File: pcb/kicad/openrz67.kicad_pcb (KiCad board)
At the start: 2 copper layers, 48 x 22 mm, 63 parts, among them K1 G6K-2F-Y DC3, K2 G6K-2F-Y DC3, Q1 DTC114EKAT146, Q2 DTC114EKAT146, U1 ESP32-C3FH4, U3 LGS5500EP, U4 S4B-XH-A(LF)(SN), X1 40MHz, X2 32.768kHz

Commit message: KiCad: archive rev-1 files, add 3D models, 0.3 mm edge clearance, cleanup
- move 2025-09-23 fabrication files and EasyEDA exports to pcb/archive/
- fetch LCSC 3D models with easyeda2kicad (tools/fetch_3d.sh); .wrl committed,
  .step gitignored; footprints repointed from dangling EASYEDA_MODELS paths
- copper-to-edge 0.30 mm with a .kicad_dru exemption for the USB-C pads
- remove two dangling vias and a 0.1 mm track stub; move two USB1 polygons
  the importer put on Edge.Cuts to F.Fab
- bottom silkscreen: OpenRZ67 Trigger v2 / 2026-09
- regenerate out/ (gerber zip, pos, BOM, PDF, renders, DRC report)
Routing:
- net VCC: vias 11 -> 10
- net +5V_VIN: vias 3 -> 2
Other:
- board text added: "OpenRZ67 Trigger v2 2026-09"
- board text removed: "EPS32-C3 Camera Trigger V1.0 2025-08-23"

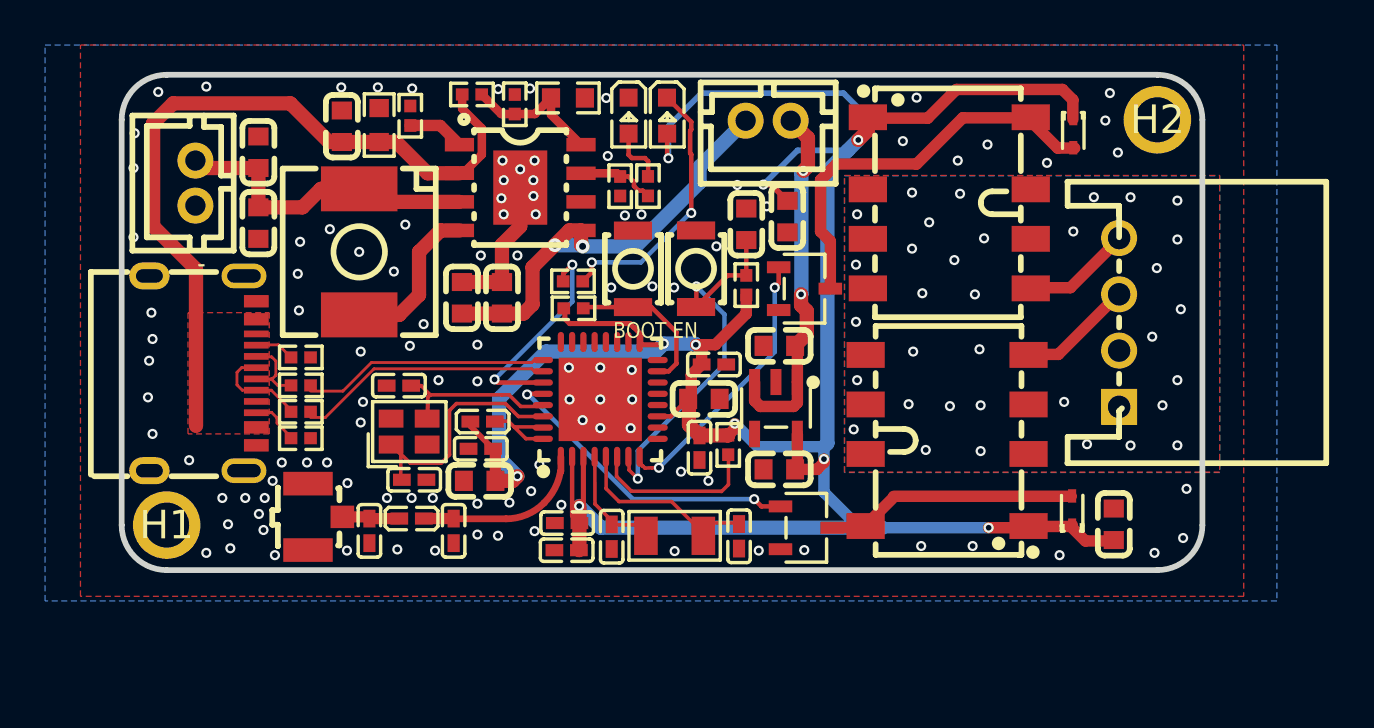
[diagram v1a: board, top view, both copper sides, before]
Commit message: KiCad: proper ERC pin types, mounting-hole symbols, courtyards, silk cleanup
- pin electrical types for ESP32-C3, LGS5500, ME6211 and USB-C; passives passive;
  PWR_FLAGs on GND/AGND/BAT+/VBUS/+5V_VIN/VDDA; ERC severities back to default
  (0 errors, 8 harmless dangling-wire warnings)
- symbol library pruned to the parts in use, embedded copies regenerated
- H1/H2: MountingHole symbols + MountingHole_2.0mm_Pad3.0 footprint, linked
- courtyards rebuilt from pads/body (+0.05 mm); 0402/0603 and overhanging
  connector silk moved to F.Fab; BOOT/EN label moved above the buttons
- tools/fetch_3d.sh bootstraps easyeda2kicad via uvx/pipx/venv; tools/export_step.sh
- DRC 0 errors / 0 unconnected / parity clean; 6 courtyard warnings remain
  where neighbours sit closer than 0.1 mm on the fabricated layout
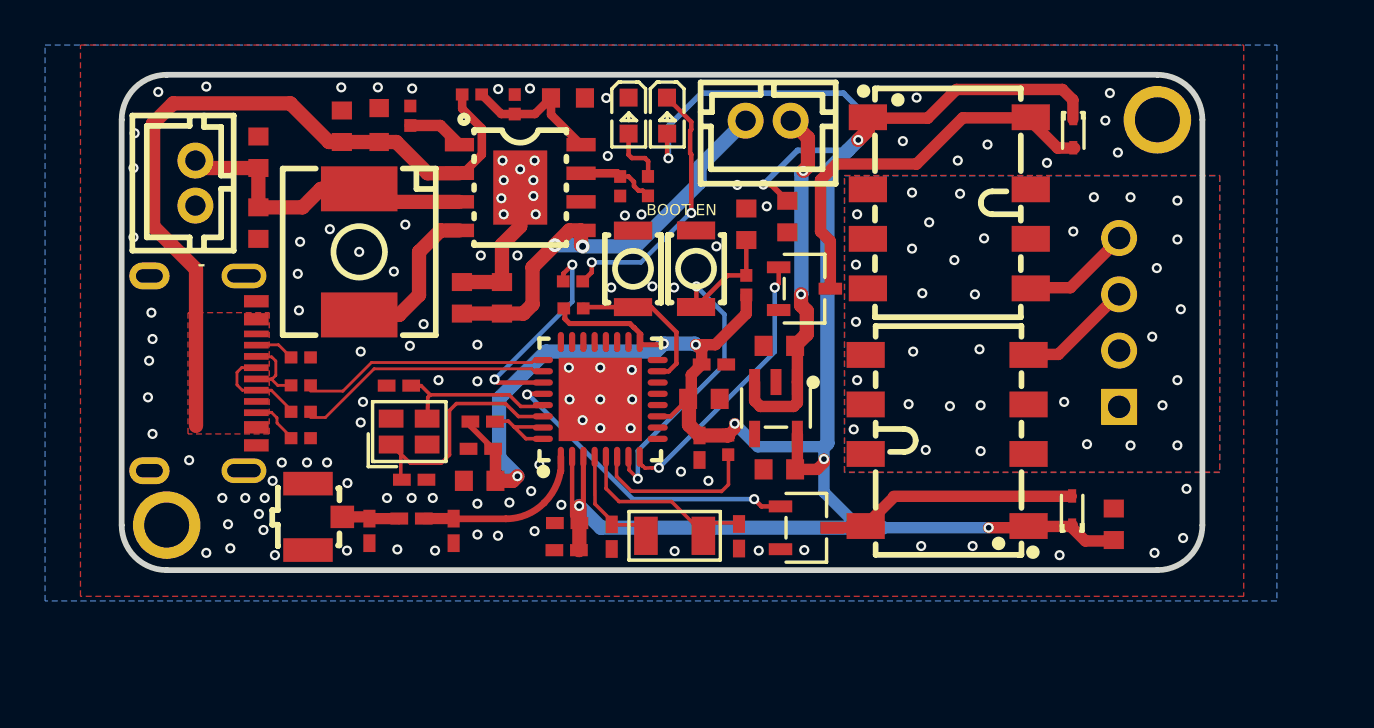
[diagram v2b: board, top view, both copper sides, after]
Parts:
- H1: value (none) -> MountingHole; footprint openrz67:Pad_e169 -> openrz67:MountingHole_2.0mm_Pad3.0
- H2: value (none) -> MountingHole; footprint openrz67:Pad_e170 -> openrz67:MountingHole_2.0mm_Pad3.0

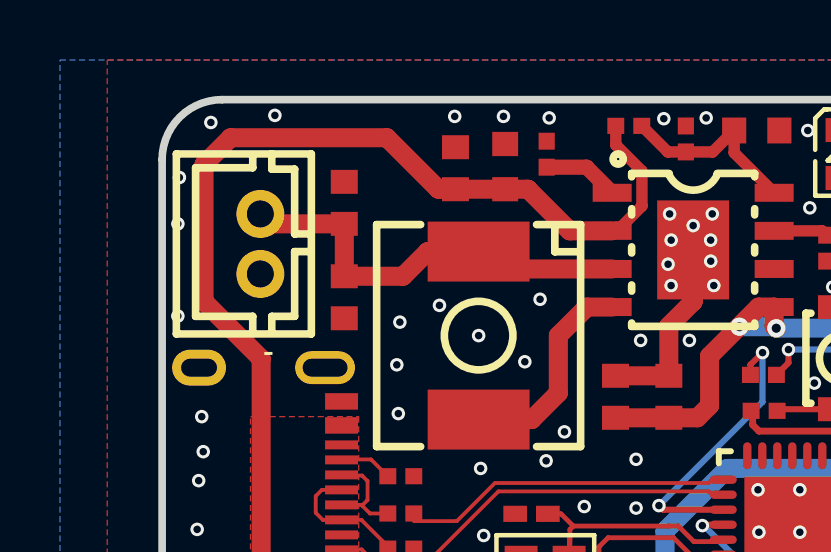
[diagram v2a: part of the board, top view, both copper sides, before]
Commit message: Rev 2: battery connector on the bottom side, facing inward
BAT1 changes from the vertical THT B2B-PH-K-S to the SMD side-entry
S2B-PH-SM4-TB (LCSC C295747) on B.Cu at the left end, opening toward the
board centre, so the cell lies flat under the PCB and plugs in without a
lead bend. BAT+ is brought down with a 0.6/0.3 via next to C22; GND uses the
bottom pour. Five GND stitching vias under the new pads removed; bottom
silkscreen labels relocated. Symbol, footprint and 3D model added to the
project libraries. DRC 0 errors, parity clean; ERC unchanged.
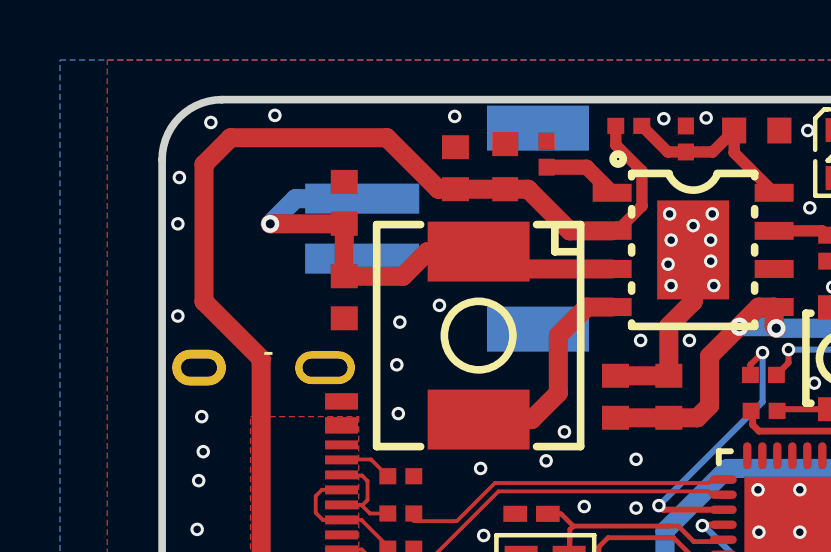
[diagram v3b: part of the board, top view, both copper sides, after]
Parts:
- BAT1: value B2B-PH-K-S(LF)(SN) -> S2B-PH-SM4-TB(LF)(SN); footprint openrz67:CONN-TH_B2B-PH-K-S -> openrz67:CONN-SMD_P2.00_S2B-PH-SM4-TB-LF-SN; moved to B.Cu
- moved BAT1 6.35 mm to (129.6, 94.3), turned to -90 degrees
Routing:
- net BAT+: track 14.2 -> 17.1 mm, vias 0 -> 1
- net GND: vias 108 -> 103

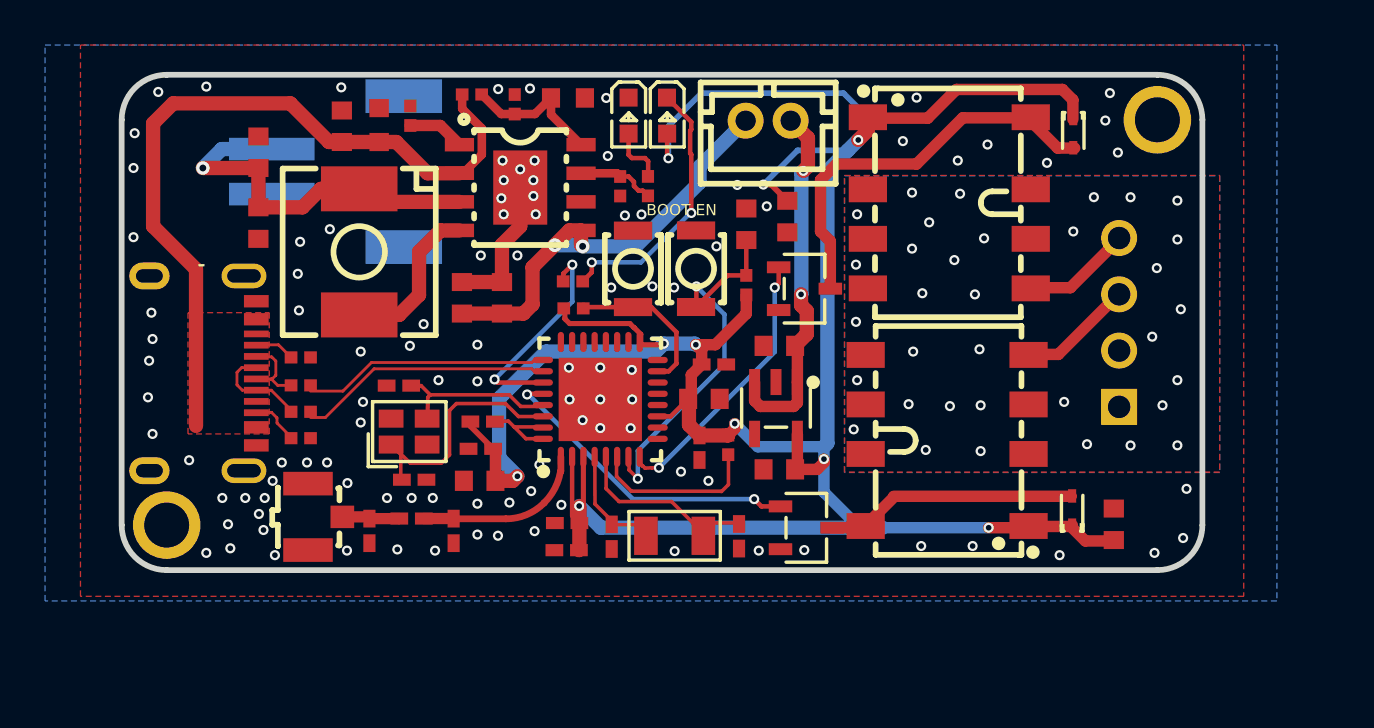
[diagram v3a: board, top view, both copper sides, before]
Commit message: Rev 2: widen board to 25 mm, add unpopulated 3-pin expansion header (GPIO4, 3V3, GND)
- new 3 mm strip along the back edge; outline rebuilt as a clean rounded rectangle
- J1 PinHeader 1x03 THT in the strip, excluded from BOM/POS; schematic Conn_01x03
  with global labels; GPIO4 = ESP32-C3 pad 9 (MTMS)
- GPIO4 routed F.Cu stub -> via -> B.Cu around the VCC track west end -> strip;
  3V3 stub to the bottom VCC track; a few GND/AGND stitching vias removed, two
  added to tie isolated top-pour islands down
- BAT1 nudged 0.15 mm off the front edge (0.3 mm copper-edge rule)
- S3 kept THT: neither SMD PH variant fits without moving C14/C28/D4
- DRC 0 errors / 0 unconnected / parity clean; ERC unchanged
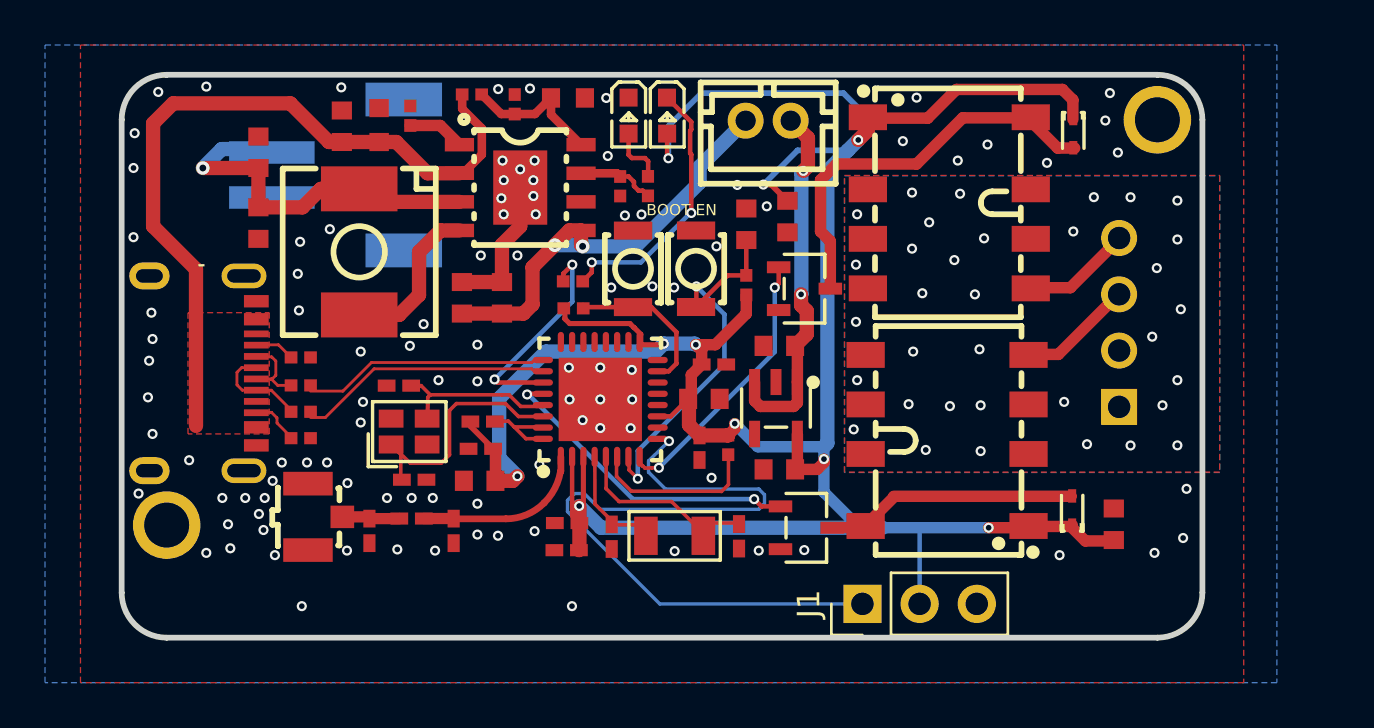
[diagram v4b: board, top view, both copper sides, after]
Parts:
- added J1: EXP (not populated), openrz67:PinHeader_1x03_P2.54mm_Vertical, F.Cu at (152.9, 113.5)
- moved BAT1 0.15 mm to (129.6, 94.5)
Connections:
- U1 pad 9: unconnected-(U1-MTMS-Pad9) -> GPIO4
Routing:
- net GPIO4: track 0.00 -> 32.9 mm, vias 0 -> 1
- net VCC: track 124.0 -> 127.4 mm
- net GND: vias 103 -> 100
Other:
- board size 48 x 22 mm -> 48 x 25 mm

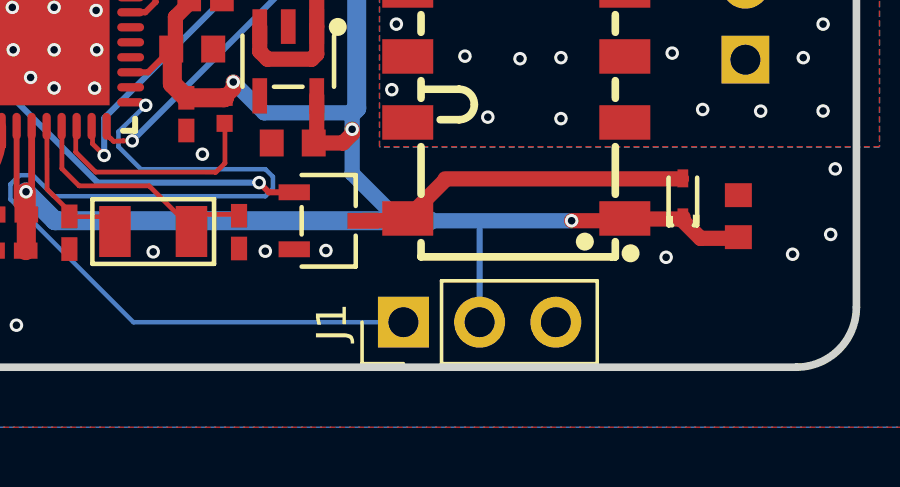
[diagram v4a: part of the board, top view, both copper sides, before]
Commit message: J1: label GPIO4 / 3V3 / GND in silkscreen on both sides, header outline to F.Fab
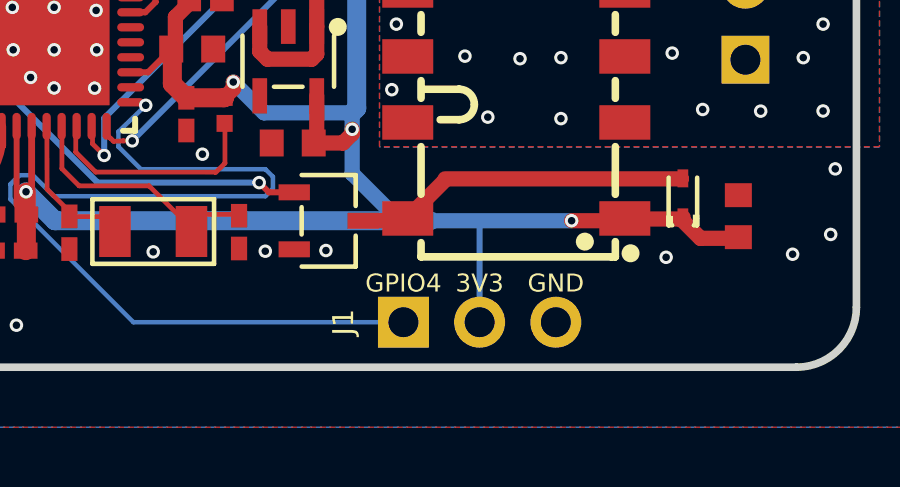
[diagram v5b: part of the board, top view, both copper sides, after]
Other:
- board text added: "3V3"
- board text added: "GPIO4"
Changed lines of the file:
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@@
 		(tags "Through hole pin header THT 1x03 2.54mm single row")
 		(property "Reference" "J1"
-			(at 0 -2.38 90)
+			(at 0 -2 90)
 			(layer "F.SilkS")
 			(effects
 				(font
-					(size 1 1)
+					(size 0.7 0.7)
 					(thickness 0.15)
 				)
@@
 		(attr through_hole exclude_from_pos_files exclude_from_bom)
 		(duplicate_pad_numbers_are_jumpers no)
+		(fp_rect
+			(start -1.77 -1.77)
+			(end 1.77 6.85)
+			(stroke
+				(width 0.05)
+				(type solid)
+			)
+			(fill no)
+			(layer "F.CrtYd")
+		)
 		(fp_line
 			(start -1.38 -1.38)
@@
 				(type solid)
 			)
-			(layer "F.SilkS")
+			(layer "F.Fab")
 		)
 		(fp_line
-			(start -1.38 0)
-			(end -1.38 -1.38)
+			(start 1.27 -1.27)
+			(end 1.27 6.35)
 			(stroke
-				(width 0.12)
+				(width 0.1)
 				(type solid)
 			)
-			(layer "F.SilkS")
+			(layer "F.Fab")
 		)
 		(fp_line
-			(start 1.38 1.27)
-			(end 1.38 6.46)
+			(start -0.635 -1.27)
+			(end 1.27 -1.27)
 			(stroke
-				(width 0.12)
+				(width 0.1)
 				(type solid)
 			)
-			(layer "F.SilkS")
+			(layer "F.Fab")
 		)
 		(fp_line
-			(start -1.38 1.27)
-			(end 1.38 1.27)
+			(start -1.27 -0.635)
+			(end -0.635 -1.27)
 			(stroke
-				(width 0.12)
+				(width 0.1)
 				(type solid)
 			)
-			(layer "F.SilkS")
+			(layer "F.Fab")
 		)
 		(fp_line
-			(start -1.38 1.27)
-			(end -1.38 6.46)
+			(start -1.38 0)
+			(end -1.38 -1.38)
 			(stroke
 				(width 0.12)
 				(type solid)
 			)
-			(layer "F.SilkS")
+			(layer "F.Fab")
 		)
 		(fp_line
-			(start -1.38 6.46)
+			(start 1.38 1.27)
 			(end 1.38 6.46)
 			(stroke
@@
 				(type solid)
 			)
-			(layer "F.SilkS")
-		)
-		(fp_rect
-			(start -1.77 -1.77)
-			(end 1.77 6.85)
-			(stroke
-				(width 0.05)
-				(type solid)
-			)
-			(fill no)
-			(layer "F.CrtYd")
+			(layer "F.Fab")
 		)
 		(fp_line
-			(start 1.27 -1.27)
-			(end 1.27 6.35)
+			(start -1.38 1.27)
+			(end 1.38 1.27)
 			(stroke
-				(width 0.1)
+				(width 0.12)
 				(type solid)
 			)
@@
 		)
 		(fp_line
-			(start -0.635 -1.27)
-			(end 1.27 -1.27)
+			(start -1.38 1.27)
+			(end -1.38 6.46)
 			(stroke
-				(width 0.1)
+				(width 0.12)
 				(type solid)
 			)
@@
 		)
 		(fp_line
-			(start -1.27 -0.635)
-			(end -0.635 -1.27)
+			(start 1.27 6.35)
+			(end -1.27 6.35)
 			(stroke
 				(width 0.1)
@@
 		)
 		(fp_line
-			(start 1.27 6.35)
-			(end -1.27 6.35)
+			(start -1.27 6.35)
+			(end -1.27 -0.635)
 			(stroke
 				(width 0.1)
@@
 		)
 		(fp_line
-			(start -1.27 6.35)
-			(end -1.27 -0.635)
+			(start -1.38 6.46)
+			(end 1.38 6.46)
 			(stroke
-				(width 0.1)
+				(width 0.12)
 				(type solid)
 			)
@@
 		)
 	)
+	(gr_text "GPIO4"
+		(at 152.9 112.2 0)
+		(layer "F.SilkS")
+		(effects
+			(font
+				(size 0.6 0.6)
+				(thickness 0.12)
+			)
+		)
+	)
+	(gr_text "3V3"
+		(at 155.44 112.2 0)
+		(layer "F.SilkS")
+		(effects
+			(font
+				(size 0.6 0.6)
+				(thickness 0.12)
+			)
+		)
+	)
+	(gr_text "GND"
+		(at 157.98 112.2 0)
+		(layer "F.SilkS")
+		(effects
+			(font
+				(size 0.6 0.6)
+				(thickness 0.12)
+			)
+		)
+	)
 	(gr_text "-"
 		(at 123.354 98.9025 0)
@@
 		)
 	)
+	(gr_text "GPIO4"
+		(at 152.9 112.2 0)
+		(layer "B.SilkS")
+		(effects
+			(font
+				(size 0.6 0.6)
+				(thickness 0.12)
+			)
+			(justify mirror)
+		)
+	)
+	(gr_text "3V3"
+		(at 155.44 112.2 0)
+		(layer "B.SilkS")
+		(effects
+			(font
+				(size 0.6 0.6)
+				(thickness 0.12)
+			)
+			(justify mirror)
+		)
+	)
+	(gr_text "GND"
+		(at 157.98 112.2 0)
+		(layer "B.SilkS")
+		(effects
+			(font
+				(size 0.6 0.6)
+				(thickness 0.12)
+			)
+			(justify mirror)
+		)
+	)
